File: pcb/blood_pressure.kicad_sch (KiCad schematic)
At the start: 2 parts, among them U1 PicoW, U2 3073

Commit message: Final schematic
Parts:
- added C1: 47u, Capacitor_SMD:C_0805_2012Metric, symbol Device:C
- added C2: 10u, Capacitor_SMD:C_0805_2012Metric, symbol Device:C
- added D1, D2, D3: LED, LED_THT:LED_D5.0mm_Clear, symbol Device:LED
- added D4: MBR1020VL, Diode_SMD:D_SOD-123F, symbol Diode:MBR1020VL
- added J1: Barrel_Jack, Connector_BarrelJack:BarrelJack_CUI_PJ-102AH_Horizontal, symbol Connector:Barrel_Jack
- added Q1: PMOS, Package_TO_SOT_SMD:SOT-23, symbol Simulation_SPICE:PMOS
- added R1: 5.6k, Resistor_SMD:R_0805_2012Metric, symbol Device:R
- added R2: 100k, Resistor_SMD:R_0805_2012Metric, symbol Device:R
- added R3: 10k, Resistor_SMD:R_0805_2012Metric, symbol Device:R
- added R4, R5, R6: 330, Resistor_SMD:R_0805_2012Metric, symbol Device:R
- added SW1: SW_Push, Button_Switch_THT:SW_PUSH_6mm, symbol Switch:SW_Push
- added SW2: SW_SPST, Button_Switch_THT:SW_PUSH_6mm, symbol Switch:SW_SPST
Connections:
- net GND: now also C1.2, C2.2, D1.1 (K), D2.1 (K), D3.1 (K), J1.2, R2.2, R3.1
- net VBUS: now also D4.2 (A), Q1.2 (G), R1.1
- net VSYS: now also C1.1, C2.1, D4.1 (K), Q1.3 (S), R2.1
- net GPIO21: now reaches U1.27 (GPIO21)
- net GPIO21: now also R1.2
- net BUTTON: now reaches U1.29 (GPIO22)
- net BUTTON: now also R3.2, SW1.2
- net ERROR LED: now reaches U1.31 (GPIO26_ADC0)
- net ERROR LED: now also R6.1
- net STATUS LED: now reaches U1.32 (GPIO27_ADC1)
- net STATUS LED: now also R5.1
- net POWER LED: now reaches U1.34 (GPIO28_ADC2)
- net POWER LED: now also R4.1
- net 3.3V: now reaches U1.36 (3V3)
- net 3.3V: now also SW1.1
- new net: J1.1, SW2.1 (A)
- new net: Q1.1 (D), SW2.2 (B)
- new net: D2.2 (A), R5.2
- new net: D1.2 (A), R4.2
- new net: D3.2 (A), R6.2
- no-connect marks 5 -> 25
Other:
- note added: "Power"
- note added: "User Interface"
- moved on the sheet: U2

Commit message: Final PCB
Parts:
- removed C1: 47u, Capacitor_SMD:C_0805_2012Metric, symbol Device:C
- removed D4: MBR1020VL, Diode_SMD:D_SOD-123F, symbol Diode:MBR1020VL
- removed R1: 5.6k, Resistor_SMD:R_0805_2012Metric, symbol Device:R
- removed R2: 100k, Resistor_SMD:R_0805_2012Metric, symbol Device:R
- added H1, H2, H3, H4: MountingHole, MountingHole:MountingHole_3.2mm_M3, symbol Mechanical:MountingHole
- SW2: footprint Button_Switch_THT:SW_PUSH_6mm -> Button_Switch_THT:SW_DIP_SPSTx01_Slide_6.7x4.1mm_W7.62mm_P2.54mm_LowProfile
- U1: footprint RPi_PicoW:RPi_Pico_SMD_TH -> pico:RPi_PicoW_SMD_TH
- U2: footprint 3073:MODULE_3073 -> rfm:rfm
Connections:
- net ERROR LED: now also U1.6 (GPIO4); no longer U1.31 (GPIO26_ADC0)
- net POWER LED: now also U1.4 (GPIO2); no longer U1.34 (GPIO28_ADC2)
- net STATUS LED: now also U1.5 (GPIO3); no longer U1.32 (GPIO27_ADC1)
- net GPIO21: no longer names the net of U1.27 (GPIO21)
- no-connect marks 25 -> 26
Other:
- note added: "Mechanical"
- moved on the sheet: J1, Q1, SW2

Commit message: Schematic
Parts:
- R4, R5, R6: value 330 -> 60
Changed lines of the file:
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@@
 			)
 		)
-		(property "Value" "330"
+		(property "Value" "60"
 			(at 176.53 73.66 90)
 			(effects
@@
 			)
 		)
-		(property "Value" "330"
+		(property "Value" "60"
 			(at 176.53 85.09 90)
 			(effects
@@
 			)
 		)
-		(property "Value" "330"
+		(property "Value" "60"
 			(at 176.53 60.96 90)
 			(effects

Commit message: Final
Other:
- company: (none) -> Cornell University
- moved on the sheet: C2, D1, D2, D3, H1, H2, H3, H4, J1, Q1, R3, R4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

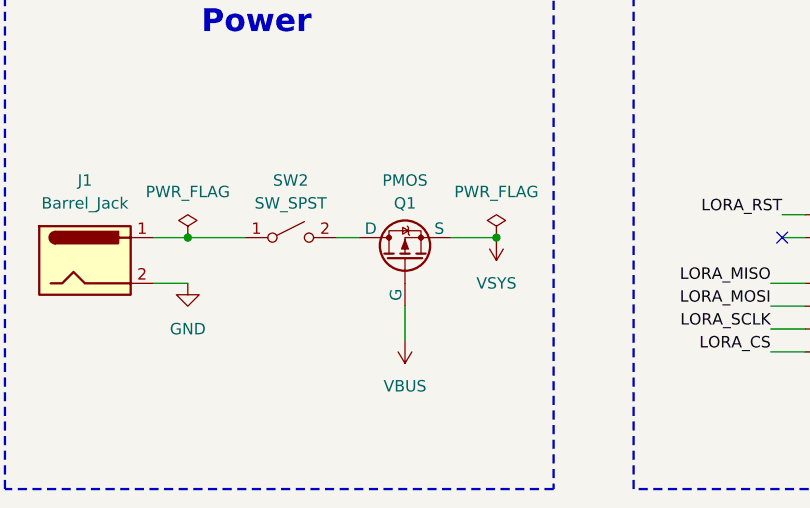
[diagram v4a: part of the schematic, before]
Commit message: process2.py and process3.py
process2 dumps raw unparsed data into txt file and works. process3 is going to parsed into csv file
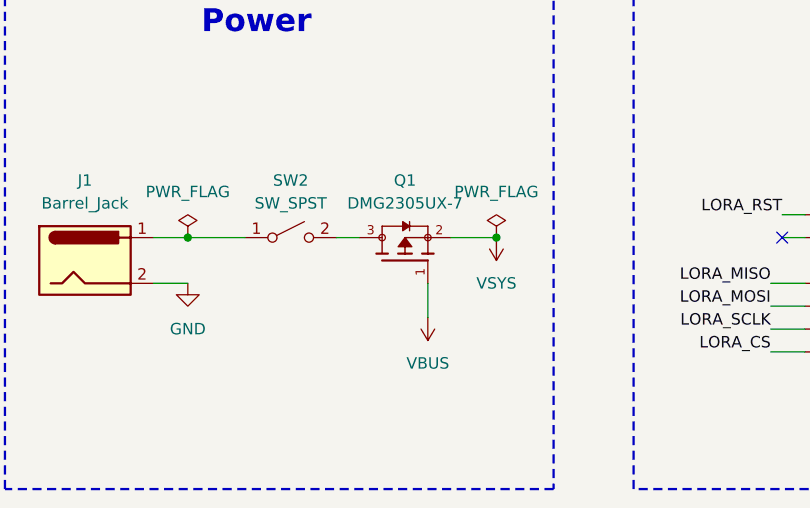
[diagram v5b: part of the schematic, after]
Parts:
- removed Q1: PMOS, Package_TO_SOT_SMD:SOT-23, symbol Simulation_SPICE:PMOS
- added Q1: DMG2305UX-7, DMG2305UX-7:SOT91P240X110-3N_DMG2305UX-7, symbol DMG2305UX-7:DMG2305UX-7
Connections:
- net VBUS: now also Q1.1
- net VSYS: now also Q1.2
- net at SW2.2 (B): now also Q1.3
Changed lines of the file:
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@@
 	(wire
 		(pts
-			(xy 146.05 147.32) (xy 146.05 151.13)
+			(xy 148.59 144.78) (xy 148.59 148.59)
 		)
 		(stroke
@@
 	)
 	(symbol
+		(lib_id "DMG2305UX-7:DMG2305UX-7")
+		(at 146.05 142.24 90)
+		(unit 1)
+		(exclude_from_sim no)
+		(in_bom yes)
+		(on_board yes)
+		(dnp no)
+		(fields_autoplaced yes)
+		(property "Reference" "Q1"
+			(at 146.05 133.35 90)
+			(effects
+				(font
+					(size 1.27 1.27)
+				)
+			)
+		)
+		(property "Value" "DMG2305UX-7"
+			(at 146.05 135.89 90)
+			(effects
+				(font
+					(size 1.27 1.27)
+				)
+			)
+		)
+		(property "Footprint" "DMG2305UX-7:SOT91P240X110-3N_DMG2305UX-7"
+			(at 146.05 142.24 0)
+			(effects
+				(font
+					(size 1.27 1.27)
+				)
+				(justify bottom)
+				(hide yes)
+			)
+		)
+		(property "Datasheet" ""
+			(at 146.05 142.24 0)
+			(effects
+				(font
+					(size 1.27 1.27)
+				)
+				(hide yes)
+			)
+		)
+		(property "Description" ""
+			(at 146.05 142.24 0)
+			(effects
+				(font
+					(size 1.27 1.27)
+				)
+				(hide yes)
+			)
+		)
+		(property "PARTREV" "09/2018"
+			(at 146.05 142.24 0)
+			(effects
+				(font
+					(size 1.27 1.27)
+				)
+				(justify bottom)
+				(hide yes)
+			)
+		)
+		(property "MANUFACTURER" "Diodes Inc."
+			(at 146.05 142.24 0)
+			(effects
+				(font
+					(size 1.27 1.27)
+				)
+				(justify bottom)
+				(hide yes)
+			)
+		)
+		(property "MAXIMUM_PACKAGE_HEIGHT" "1.1mm"
+			(at 146.05 142.24 0)
+			(effects
+				(font
+					(size 1.27 1.27)
+				)
+				(justify bottom)
+				(hide yes)
+			)
+		)
+		(property "STANDARD" "IPC-7351B"
+			(at 146.05 142.24 0)
+			(effects
+				(font
+					(size 1.27 1.27)
+				)
+				(justify bottom)
+				(hide yes)
+			)
+		)
+		(pin "3"
+		)
+		(pin "2"
+		)
+		(pin "1"
+		)
+		(instances
+			(project ""
+				(path "/fff1fc37-b089-485b-b67d-533be3f01cc9"
+					(reference "Q1")
+					(unit 1)
+				)
+			)
+		)
+	)
+	(symbol
 		(lib_id "power:GND")
 		(at 205.74 100.33 0)
@@
 	)
 	(symbol
-		(lib_id "Simulation_SPICE:PMOS")
-		(at 146.05 142.24 90)
-		(unit 1)
-		(exclude_from_sim no)
-		(in_bom yes)
-		(on_board yes)
-		(dnp no)
-		(fields_autoplaced yes)
-		(property "Reference" "Q1"
-			(at 146.05 135.89 90)
-			(effects
-				(font
-					(size 1.27 1.27)
-				)
-			)
-		)
-		(property "Value" "PMOS"
-			(at 146.05 133.35 90)
-			(effects
-				(font
-					(size 1.27 1.27)
-				)
-			)
-		)
-		(property "Footprint" "Package_TO_SOT_SMD:SOT-23"
-			(at 143.51 137.16 0)
-			(effects
-				(font
-					(size 1.27 1.27)
-				)
-				(hide yes)
-			)
-		)
-		(property "Datasheet" "https://ngspice.sourceforge.io/docs/ngspice-html-manual/manual.xhtml#cha_MOSFETs"
-			(at 158.75 142.24 0)
-			(effects
-				(font
-					(size 1.27 1.27)
-				)
-				(hide yes)
-			)
-		)
-		(property "Description" "P-MOSFET transistor, drain/source/gate"
-			(at 146.05 142.24 0)
-			(effects
-				(font
-					(size 1.27 1.27)
-				)
-				(hide yes)
-			)
-		)
-		(property "Sim.Device" "PMOS"
-			(at 163.195 142.24 0)
-			(effects
-				(font
-					(size 1.27 1.27)
-				)
-				(hide yes)
-			)
-		)
-		(property "Sim.Type" "VDMOS"
-			(at 165.1 142.24 0)
-			(effects
-				(font
-					(size 1.27 1.27)
-				)
-				(hide yes)
-			)
-		)
-		(property "Sim.Pins" "1=D 2=G 3=S"
-			(at 161.29 142.24 0)
-			(effects
-				(font
-					(size 1.27 1.27)
-				)
-				(hide yes)
-			)
-		)
-		(pin "2"
-		)
-		(pin "3"
-		)
-		(pin "1"
-		)
-		(instances
-			(project ""
-				(path "/fff1fc37-b089-485b-b67d-533be3f01cc9"
-					(reference "Q1")
-					(unit 1)
-				)
-			)
-		)
-	)
-	(symbol
 		(lib_id "Device:LED")
 		(at 120.65 95.25 0)
@@
 	(symbol
 		(lib_id "power:VBUS")
-		(at 146.05 151.13 180)
+		(at 148.59 148.59 180)
 		(unit 1)
 		(exclude_from_sim no)
@@
 		(fields_autoplaced yes)
 		(property "Reference" "#PWR012"
-			(at 146.05 147.32 0)
+			(at 148.59 144.78 0)
 			(effects
 				(font
@@
 		)
 		(property "Value" "VBUS"
-			(at 146.05 156.21 0)
+			(at 148.59 153.67 0)
 			(effects
 				(font
@@
 		)
 		(property "Footprint" ""
-			(at 146.05 151.13 0)
+			(at 148.59 148.59 0)
 			(effects
 				(font
@@
 		)
 		(property "Datasheet" ""
-			(at 146.05 151.13 0)
+			(at 148.59 148.59 0)
 			(effects
 				(font
@@
 		)
 		(property "Description" "Power symbol creates a global label with name \"VBUS\""
-			(at 146.05 151.13 0)
-			(effects
-				(font
+			(at 148.59 148.59 0)
+			(effects
+				(font

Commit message: Read Me Files
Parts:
- Q1: footprint DMG2305UX-7:SOT91P240X110-3N_DMG2305UX-7 -> DMG2305UX_7:SOT91P240X110-3N_DMG2305UX-7
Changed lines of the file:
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@@
 			)
 		)
-		(property "Footprint" "DMG2305UX-7:SOT91P240X110-3N_DMG2305UX-7"
+		(property "Footprint" "DMG2305UX_7:SOT91P240X110-3N_DMG2305UX-7"
 			(at 146.05 142.24 0)
 			(effects
